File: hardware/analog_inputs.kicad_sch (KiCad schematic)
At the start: 6 parts

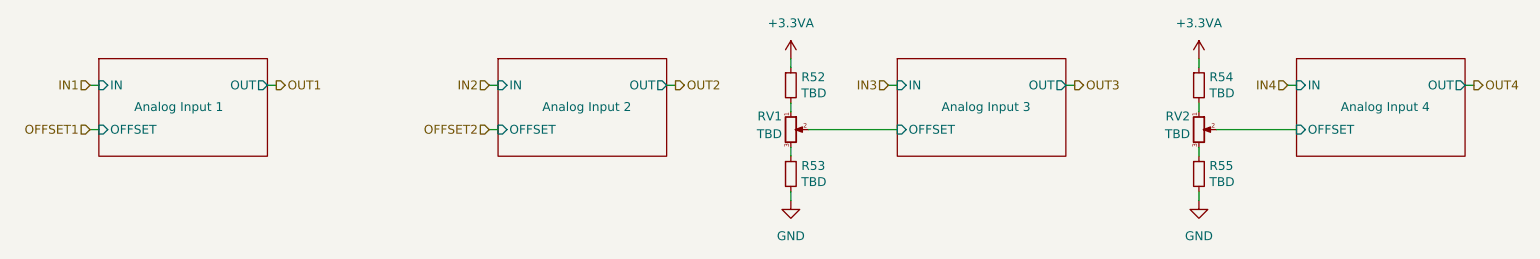
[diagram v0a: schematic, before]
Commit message: Improve the schematic according to the feedback
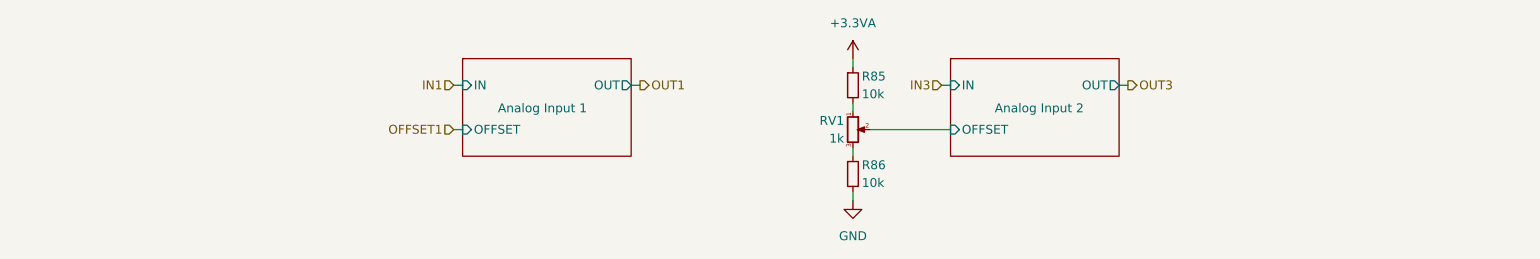
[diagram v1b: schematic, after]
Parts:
- removed R54, R55: TBD, Resistor_SMD:R_0603_1608Metric, symbol Device:R_Small
- removed RV2: TBD, Potentiometer_SMD:Potentiometer_Bourns_3214J_Horizontal, symbol Device:R_Potentiometer_Small
- R85: renamed from R52; value TBD -> 10k
- R86: renamed from R53; value TBD -> 10k
- RV1: value TBD -> 1k
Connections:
- net Analog Input 3/OFFSET renamed Analog Input 2/OFFSET
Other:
- removed sheet Analog Input 3
- removed sheet Analog Input 4
- moved on the sheet: R85, R86, RV1

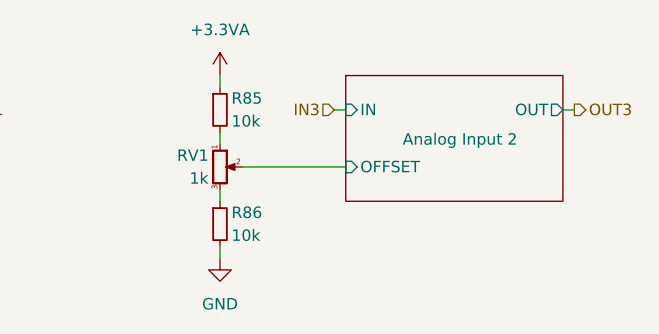
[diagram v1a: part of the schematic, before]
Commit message: Add high-side drivers to the fans and pumps
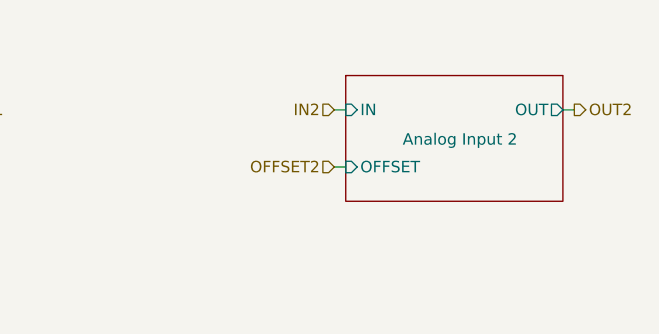
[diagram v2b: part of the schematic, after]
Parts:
- removed R85, R86: 10k, Resistor_SMD:R_0603_1608Metric, symbol Device:R_Small
- removed RV1: 1k, Potentiometer_SMD:Potentiometer_Bourns_3214J_Horizontal, symbol Device:R_Potentiometer_Small
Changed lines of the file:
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@@
   (title_block
     (title "Analog Inputs")
-    (date "2023-07-01")
+    (date "2023-09-20")
     (rev "${REVISION}")
     (company "Author: I. Kajdan")
@@
     (stroke (width 0) (type default))
   )
-  (wire (pts (xy 165.1 101.6) (xy 176.53 101.6))
+  (wire (pts (xy 175.26 101.6) (xy 176.53 101.6))
     (stroke (width 0) (type default))
   )
@@
     (stroke (width 0) (type default))
   )
-  (wire (pts (xy 162.56 97.79) (xy 162.56 99.06))
-    (stroke (width 0) (type default))
-  )
   (wire (pts (xy 130.81 95.25) (xy 132.08 95.25))
-    (stroke (width 0) (type default))
-  )
-  (wire (pts (xy 162.56 110.49) (xy 162.56 111.76))
-    (stroke (width 0) (type default))
-  )
-  (wire (pts (xy 162.56 91.44) (xy 162.56 92.71))
     (stroke (width 0) (type default))
   )
@@
     (stroke (width 0) (type default))
   )
-  (wire (pts (xy 162.56 104.14) (xy 162.56 105.41))
+  (wire (pts (xy 200.66 95.25) (xy 201.93 95.25))
     (stroke (width 0) (type default))
   )
-  (wire (pts (xy 200.66 95.25) (xy 201.93 95.25))
-    (stroke (width 0) (type default))
+  (hierarchical_label "OFFSET2" (shape input) (at 175.26 101.6 180) (fields_autoplaced)
+    (effects (font (size 1.27 1.27)) (justify right))
   )
   (hierarchical_label "OFFSET1" (shape input) (at 105.41 101.6 180) (fields_autoplaced)
     (effects (font (size 1.27 1.27)) (justify right))
   )
-  (hierarchical_label "IN3" (shape input) (at 175.26 95.25 180) (fields_autoplaced)
+  (hierarchical_label "IN2" (shape input) (at 175.26 95.25 180) (fields_autoplaced)
     (effects (font (size 1.27 1.27)) (justify right))
   )
-  (hierarchical_label "OUT3" (shape output) (at 201.93 95.25 0) (fields_autoplaced)
+  (hierarchical_label "OUT2" (shape output) (at 201.93 95.25 0) (fields_autoplaced)
     (effects (font (size 1.27 1.27)) (justify left))
   )
@@
     (effects (font (size 1.27 1.27)) (justify left))
   )
-  (symbol (lib_id "Device:R_Small") (at 162.56 107.95 0) (unit 1)
-    (in_bom yes) (on_board yes) (dnp no)
-    (property "Reference" "R86" (at 163.83 106.68 0)
-      (effects (font (size 1.27 1.27)) (justify left))
-    )
-    (property "Value" "10k" (at 163.83 109.22 0)
-      (effects (font (size 1.27 1.27)) (justify left))
-    )
-    (property "Footprint" "Resistor_SMD:R_0603_1608Metric" (at 162.56 107.95 0)
-      (effects (font (size 1.27 1.27)) hide)
-    )
-    (property "Datasheet" "~" (at 162.56 107.95 0)
-      (effects (font (size 1.27 1.27)) hide)
-    )
-    (pin "1")
-    (pin "2")
-    (instances
-      (project "rearbox"
-        (path "/b652b05a-4e3d-4ad1-b032-18886abe7d45/264ec557-c33b-4d6e-8249-7c546f6f500a"
-          (reference "R86") (unit 1)
-        )
-      )
-      (project "apps"
-        (path "/fc4ad874-c922-4070-89f9-7262080469d8/00000000-0000-0000-0000-00006068dc5c"
-          (reference "R8") (unit 1)
-        )
-      )
-    )
-  )
-  (symbol (lib_id "Device:R_Small") (at 162.56 95.25 0) (unit 1)
-    (in_bom yes) (on_board yes) (dnp no)
-    (property "Reference" "R85" (at 163.83 93.98 0)
-      (effects (font (size 1.27 1.27)) (justify left))
-    )
-    (property "Value" "10k" (at 163.83 96.52 0)
-      (effects (font (size 1.27 1.27)) (justify left))
-    )
-    (property "Footprint" "Resistor_SMD:R_0603_1608Metric" (at 162.56 95.25 0)
-      (effects (font (size 1.27 1.27)) hide)
-    )
-    (property "Datasheet" "~" (at 162.56 95.25 0)
-      (effects (font (size 1.27 1.27)) hide)
-    )
-    (pin "1")
-    (pin "2")
-    (instances
-      (project "rearbox"
-        (path "/b652b05a-4e3d-4ad1-b032-18886abe7d45/264ec557-c33b-4d6e-8249-7c546f6f500a"
-          (reference "R85") (unit 1)
-        )
-      )
-      (project "apps"
-        (path "/fc4ad874-c922-4070-89f9-7262080469d8/00000000-0000-0000-0000-00006068dc5c"
-          (reference "R7") (unit 1)
-        )
-      )
-    )
-  )
-  (symbol (lib_id "Device:R_Potentiometer_Small") (at 162.56 101.6 0) (unit 1)
-    (in_bom yes) (on_board yes) (dnp no)
-    (property "Reference" "RV1" (at 161.29 100.33 0)
-      (effects (font (size 1.27 1.27)) (justify right))
-    )
-    (property "Value" "1k" (at 161.29 102.87 0)
-      (effects (font (size 1.27 1.27)) (justify right))
-    )
-    (property "Footprint" "Potentiometer_SMD:Potentiometer_Bourns_3214J_Horizontal" (at 162.56 101.6 0)
-      (effects (font (size 1.27 1.27)) hide)
-    )
-    (property "Datasheet" "~" (at 162.56 101.6 0)
-      (effects (font (size 1.27 1.27)) hide)
-    )
-    (pin "1")
-    (pin "2")
-    (pin "3")
-    (instances
-      (project "rearbox"
-        (path "/b652b05a-4e3d-4ad1-b032-18886abe7d45/264ec557-c33b-4d6e-8249-7c546f6f500a"
-          (reference "RV1") (unit 1)
-        )
-      )
-      (project "apps"
-        (path "/fc4ad874-c922-4070-89f9-7262080469d8/00000000-0000-0000-0000-00006068dc5c"
-          (reference "RV1") (unit 1)
-        )
-      )
-    )
-  )
-  (symbol (lib_id "power:GND") (at 162.56 111.76 0) (unit 1)
-    (in_bom yes) (on_board yes) (dnp no)
-    (property "Reference" "#PWR0127" (at 162.56 118.11 0)
-      (effects (font (size 1.27 1.27)) hide)
-    )
-    (property "Value" "GND" (at 162.56 116.84 0)
-      (effects (font (size 1.27 1.27)))
-    )
-    (property "Footprint" "" (at 162.56 111.76 0)
-      (effects (font (size 1.27 1.27)) hide)
-    )
-    (property "Datasheet" "" (at 162.56 111.76 0)
-      (effects (font (size 1.27 1.27)) hide)
-    )
-    (pin "1")
-    (instances
-      (project "rearbox"
-        (path "/b652b05a-4e3d-4ad1-b032-18886abe7d45/264ec557-c33b-4d6e-8249-7c546f6f500a"
-          (reference "#PWR0127") (unit 1)
-        )
-      )
-      (project "apps"
-        (path "/fc4ad874-c922-4070-89f9-7262080469d8/00000000-0000-0000-0000-00006068dc5c"
-          (reference "#PWR012") (unit 1)
-        )
-      )
-    )
-  )
-  (symbol (lib_id "power:+3.3VA") (at 162.56 91.44 0) (unit 1)
-    (in_bom yes) (on_board yes) (dnp no)
-    (property "Reference" "#PWR?" (at 162.56 95.25 0)
-      (effects (font (size 1.27 1.27)) hide)
-    )
-    (property "Value" "+3.3VA" (at 162.56 86.36 0)
-      (effects (font (size 1.27 1.27)))
-    )
-    (property "Footprint" "" (at 162.56 91.44 0)
-      (effects (font (size 1.27 1.27)) hide)
-    )
-    (property "Datasheet" "" (at 162.56 91.44 0)
-      (effects (font (size 1.27 1.27)) hide)
-    )
-    (pin "1")
-    (instances
-      (project "rearbox"
-        (path "/b652b05a-4e3d-4ad1-b032-18886abe7d45/7045152e-d7a2-42d7-9b15-138e7f2928ca"
-          (reference "#PWR?") (unit 1)
-        )
-        (path "/b652b05a-4e3d-4ad1-b032-18886abe7d45"
-          (reference "#PWR?") (unit 1)
-        )
-        (path "/b652b05a-4e3d-4ad1-b032-18886abe7d45/264ec557-c33b-4d6e-8249-7c546f6f500a"
-          (reference "#PWR0126") (unit 1)
-        )
-        (path "/b652b05a-4e3d-4ad1-b032-18886abe7d45/264ec557-c33b-4d6e-8249-7c546f6f500a/2ebbc597-c328-4a79-a9b9-9ad195d56b16"
-          (reference "#PWR0198") (unit 1)
-        )
-        (path "/b652b05a-4e3d-4ad1-b032-18886abe7d45/264ec557-c33b-4d6e-8249-7c546f6f500a/388565cf-56d9-4d05-bbee-ba12b3a092d4"
-          (reference "#PWR0216") (unit 1)
-        )
-      )
-    )
-  )
   (sheet (at 106.68 91.44) (size 24.13 13.97)
